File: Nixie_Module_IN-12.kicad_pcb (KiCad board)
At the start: 2 copper layers, 20 x 40 mm, 43 parts, among them J1 CONN_01X07, J3 CONN_01X02, J4 CONN_01X02, Q1 Q_NPN_BEC, Q10 Q_NPN_BEC, Q11 Q_NPN_BEC, Q2 Q_NPN_BEC, Q3 Q_NPN_BEC, Q4 Q_NPN_BEC, Q5 Q_NPN_BEC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

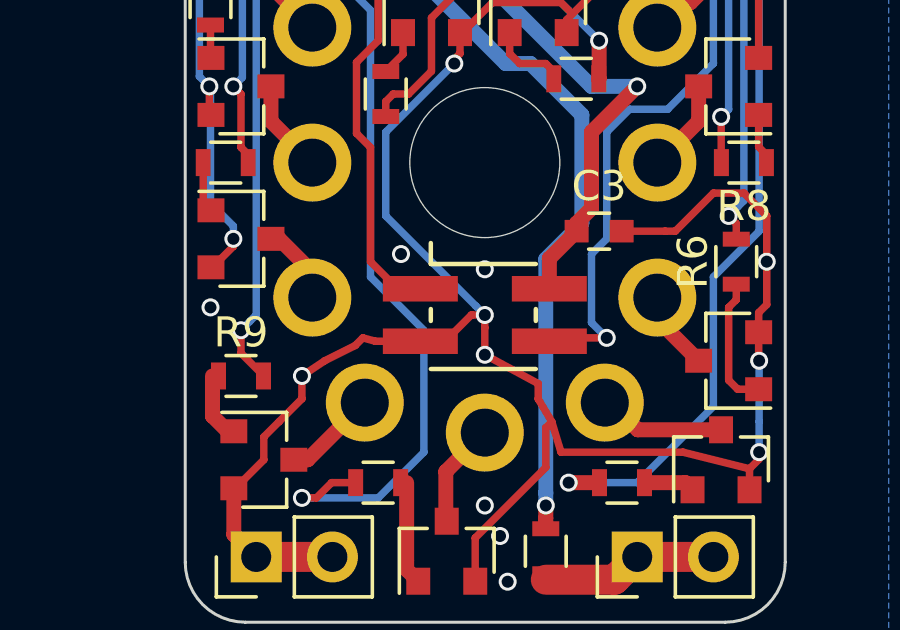
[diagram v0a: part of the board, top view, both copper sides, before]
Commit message: change to WS2812b
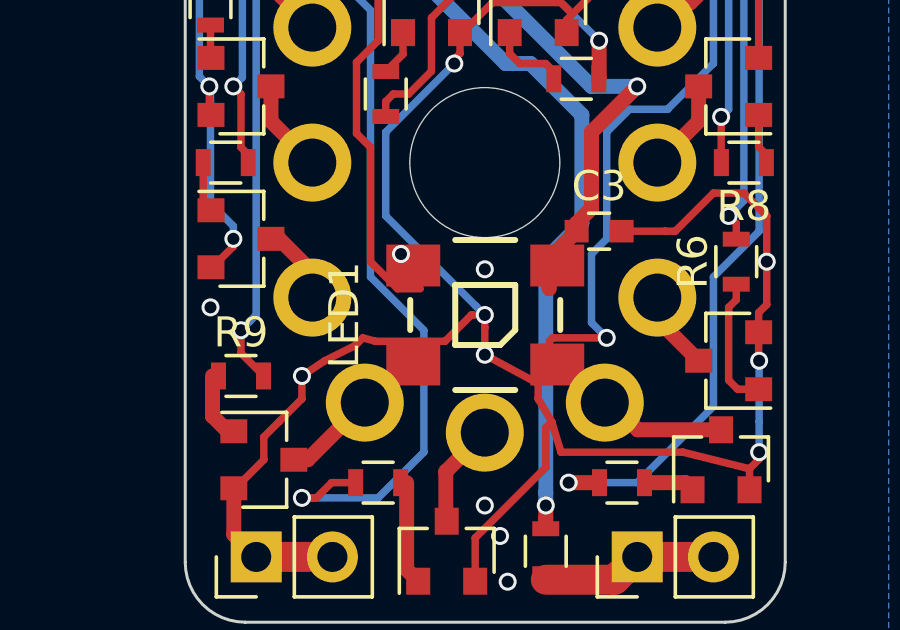
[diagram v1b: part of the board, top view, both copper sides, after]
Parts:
- removed U1: SK6812mini, FidgetSpinner:SK6812MINI
- added LED1: WS2812B, WS2812b:WS2812B, F.Cu at (79.3, 91.9)
- R1: value R -> 15k
- R14, R15, R16, R17, R18, R19, R2: value R -> 10k
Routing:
- net GND: vias 31 -> 30
- net +5V: vias 3 -> 4

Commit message: update footprint
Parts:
- LED1: value WS2812B -> VAL**
- moved LED1 0.25 mm to (79.3, 91.7), turned to 180 degrees
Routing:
- net +5V: track 51.3 -> 49.0 mm
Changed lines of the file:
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@@
     (thickness 1.6)
     (drawings 43)
-    (tracks 630)
+    (tracks 628)
     (zones 0)
     (modules 43)
@@
     (38 B.Mask user hide)
     (39 F.Mask user hide)
-    (40 Dwgs.User user hide)
+    (40 Dwgs.User user)
     (41 Cmts.User user hide)
     (42 Eco1.User user hide)
@@
     (add_net +HV)
   )
+  (module WS2812b:WS2812B (layer F.Cu)
+    (at 79.262 91.694 180)
+    (fp_text reference LED1 (at 0 -4.7 180) (layer F.SilkS)
+      (effects (font (size 1 1) (thickness 0.2)))
+    )
+    (fp_text value VAL** (at 0 4.8 180) (layer F.SilkS) hide
+      (effects (font (size 1 1) (thickness 0.2)))
+    )
+    (fp_line (start -2.49936 2.49936) (end -2.49936 -2.49936) (layer Dwgs.User) (width 0.2))
+    (fp_line (start 2.5 -2.5) (end 2.5 2.5) (layer Dwgs.User) (width 0.2))
+    (fp_line (start 2.1 2.7) (end 1.2 2.7) (layer Dwgs.User) (width 0.2))
+    (fp_line (start 2.1 1.8) (end 2.1 2.7) (layer Dwgs.User) (width 0.2))
+    (fp_line (start 1.2 1.8) (end 2.1 1.8) (layer Dwgs.User) (width 0.2))
+    (fp_line (start 1.2 2.7) (end 1.2 1.8) (layer Dwgs.User) (width 0.2))
+    (fp_line (start -1.2 2.7) (end -2.1 2.7) (layer Dwgs.User) (width 0.2))
+    (fp_line (start -1.2 1.8) (end -1.2 2.7) (layer Dwgs.User) (width 0.2))
+    (fp_line (start -2.1 1.8) (end -1.2 1.8) (layer Dwgs.User) (width 0.2))
+    (fp_line (start -2.1 2.7) (end -2.1 1.8) (layer Dwgs.User) (width 0.2))
+    (fp_line (start 2.1 -1.8) (end 2.1 -2.7) (layer Dwgs.User) (width 0.2))
+    (fp_line (start 1.2 -1.8) (end 2.1 -1.8) (layer Dwgs.User) (width 0.2))
+    (fp_line (start 1.2 -2.7) (end 1.2 -1.8) (layer Dwgs.User) (width 0.2))
+    (fp_line (start 2.1 -2.7) (end 1.2 -2.7) (layer Dwgs.User) (width 0.2))
+    (fp_line (start -2.1 -1.8) (end -2.1 -2.7) (layer Dwgs.User) (width 0.2))
+    (fp_line (start -1.2 -1.8) (end -2.1 -1.8) (layer Dwgs.User) (width 0.2))
+    (fp_line (start -1.2 -2.7) (end -1.2 -1.8) (layer Dwgs.User) (width 0.2))
+    (fp_line (start -2.1 -2.7) (end -1.2 -2.7) (layer Dwgs.User) (width 0.2))
+    (fp_line (start -2.5 -2.5) (end -2.1 -2.5) (layer Dwgs.User) (width 0.2))
+    (fp_line (start -1.2 -2.5) (end 1.2 -2.5) (layer Dwgs.User) (width 0.2))
+    (fp_line (start 2.1 -2.5) (end 2.5 -2.5) (layer Dwgs.User) (width 0.2))
+    (fp_line (start -2.5 2.5) (end -2.1 2.5) (layer Dwgs.User) (width 0.2))
+    (fp_line (start -1.2 2.5) (end 1.2 2.5) (layer Dwgs.User) (width 0.2))
+    (fp_line (start 2.1 2.5) (end 2.5 2.5) (layer Dwgs.User) (width 0.2))
+    (fp_line (start -0.5 -2.5) (end 0.5 -2.5) (layer F.SilkS) (width 0.2))
+    (fp_line (start 2.5 -1) (end 2.5 1) (layer F.SilkS) (width 0.2))
+    (fp_line (start -0.5 2.5) (end 0.5 2.5) (layer F.SilkS) (width 0.2))
+    (fp_line (start -2.5 -1) (end -2.5 1) (layer F.SilkS) (width 0.2))
+    (fp_line (start -1 0.5) (end -1 -1) (layer F.SilkS) (width 0.2))
+    (fp_line (start -0.5 1) (end -1 0.5) (layer F.SilkS) (width 0.2))
+    (fp_line (start 1 1) (end -0.5 1) (layer F.SilkS) (width 0.2))
+    (fp_line (start 1 -1) (end 1 1) (layer F.SilkS) (width 0.2))
+    (fp_line (start -1 -1) (end 1 -1) (layer F.SilkS) (width 0.2))
+    (pad 4 smd rect (at 1.65 2.4 180) (size 1 1.5) (layers F.Cu F.Paste F.Mask)
+      (net 42 /LED_DIN))
+    (pad 3 smd rect (at -1.65 2.4 180) (size 1 1.5) (layers F.Cu F.Paste F.Mask)
+      (net 2 GND))
+    (pad 2 smd rect (at -1.65 -2.4 180) (size 1 1.5) (layers F.Cu F.Paste F.Mask)
+      (net 43 /LED_DOUT))
+    (pad 1 smd rect (at 1.65 -2.4 180) (size 1 1.5) (layers F.Cu F.Paste F.Mask)
+      (net 1 +5V))
+  )
   (module R_SMD:R_0603 (layer F.Cu)
     (at 75.946 84.582 270)
@@
            (xy 0 0.75) (xy -0.5 0.75) (xy -0.5 -0.75) (xy 0 -0.75)) (width 0))
       ))
-  )
-  (module WS2812b:WS2812B (layer F.Cu)
-    (at 79.262 91.948 90)
-    (fp_text reference LED1 (at 0 -4.7 90) (layer F.SilkS)
-      (effects (font (size 1 1) (thickness 0.2)))
-    )
-    (fp_text value WS2812B (at 0 4.8 90) (layer F.SilkS) hide
-      (effects (font (size 1 1) (thickness 0.2)))
-    )
-    (fp_line (start -1 -1) (end 1 -1) (layer F.SilkS) (width 0.2))
-    (fp_line (start 1 -1) (end 1 1) (layer F.SilkS) (width 0.2))
-    (fp_line (start 1 1) (end -0.5 1) (layer F.SilkS) (width 0.2))
-    (fp_line (start -0.5 1) (end -1 0.5) (layer F.SilkS) (width 0.2))
-    (fp_line (start -1 0.5) (end -1 -1) (layer F.SilkS) (width 0.2))
-    (fp_line (start -2.5 -1) (end -2.5 1) (layer F.SilkS) (width 0.2))
-    (fp_line (start -0.5 2.5) (end 0.5 2.5) (layer F.SilkS) (width 0.2))
-    (fp_line (start 2.5 -1) (end 2.5 1) (layer F.SilkS) (width 0.2))
-    (fp_line (start -0.5 -2.5) (end 0.5 -2.5) (layer F.SilkS) (width 0.2))
-    (fp_line (start 2.1 2.5) (end 2.5 2.5) (layer Dwgs.User) (width 0.2))
-    (fp_line (start -1.2 2.5) (end 1.2 2.5) (layer Dwgs.User) (width 0.2))
-    (fp_line (start -2.5 2.5) (end -2.1 2.5) (layer Dwgs.User) (width 0.2))
-    (fp_line (start 2.1 -2.5) (end 2.5 -2.5) (layer Dwgs.User) (width 0.2))
-    (fp_line (start -1.2 -2.5) (end 1.2 -2.5) (layer Dwgs.User) (width 0.2))
-    (fp_line (start -2.5 -2.5) (end -2.1 -2.5) (layer Dwgs.User) (width 0.2))
-    (fp_line (start -2.1 -2.7) (end -1.2 -2.7) (layer Dwgs.User) (width 0.2))
-    (fp_line (start -1.2 -2.7) (end -1.2 -1.8) (layer Dwgs.User) (width 0.2))
-    (fp_line (start -1.2 -1.8) (end -2.1 -1.8) (layer Dwgs.User) (width 0.2))
-    (fp_line (start -2.1 -1.8) (end -2.1 -2.7) (layer Dwgs.User) (width 0.2))
-    (fp_line (start 2.1 -2.7) (end 1.2 -2.7) (layer Dwgs.User) (width 0.2))
-    (fp_line (start 1.2 -2.7) (end 1.2 -1.8) (layer Dwgs.User) (width 0.2))
-    (fp_line (start 1.2 -1.8) (end 2.1 -1.8) (layer Dwgs.User) (width 0.2))
-    (fp_line (start 2.1 -1.8) (end 2.1 -2.7) (layer Dwgs.User) (width 0.2))
-    (fp_line (start -2.1 2.7) (end -2.1 1.8) (layer Dwgs.User) (width 0.2))
-    (fp_line (start -2.1 1.8) (end -1.2 1.8) (layer Dwgs.User) (width 0.2))
-    (fp_line (start -1.2 1.8) (end -1.2 2.7) (layer Dwgs.User) (width 0.2))
-    (fp_line (start -1.2 2.7) (end -2.1 2.7) (layer Dwgs.User) (width 0.2))
-    (fp_line (start 1.2 2.7) (end 1.2 1.8) (layer Dwgs.User) (width 0.2))
-    (fp_line (start 1.2 1.8) (end 2.1 1.8) (layer Dwgs.User) (width 0.2))
-    (fp_line (start 2.1 1.8) (end 2.1 2.7) (layer Dwgs.User) (width 0.2))
-    (fp_line (start 2.1 2.7) (end 1.2 2.7) (layer Dwgs.User) (width 0.2))
-    (fp_line (start 2.5 -2.5) (end 2.5 2.5) (layer Dwgs.User) (width 0.2))
-    (fp_line (start -2.49936 2.49936) (end -2.49936 -2.49936) (layer Dwgs.User) (width 0.2))
-    (pad 1 smd rect (at 1.65 -2.4 90) (size 1.4 1.8) (layers F.Cu F.Paste F.Mask)
-      (net 1 +5V))
-    (pad 2 smd rect (at -1.65 -2.4 90) (size 1.4 1.8) (layers F.Cu F.Paste F.Mask)
-      (net 43 /LED_DOUT))
-    (pad 3 smd rect (at -1.65 2.4 90) (size 1.4 1.8) (layers F.Cu F.Paste F.Mask)
-      (net 2 GND))
-    (pad 4 smd rect (at 1.65 2.4 90) (size 1.4 1.8) (layers F.Cu F.Paste F.Mask)
-      (net 42 /LED_DIN))
   )
   (gr_text ADDR3 (at 75.184 75.438) (layer B.SilkS)
@@
   (segment (start 74.168 72.644) (end 74.676 72.644) (width 0.25) (layer F.Cu) (net 1))
   (segment (start 73.356 72.644) (end 74.168 72.644) (width 0.25) (layer F.Cu) (net 1))
-  (segment (start 81.398 90.064) (end 82.308 89.154) (width 0.5) (layer F.Cu) (net 1) (status 20))
-  (segment (start 81.398 91.073) (end 81.398 90.064) (width 0.5) (layer F.Cu) (net 1))
   (segment (start 82.308 88.912) (end 82.308 89.154) (width 0.5) (layer F.Cu) (net 1) (status 30))
   (segment (start 82.296 88.9) (end 82.308 88.912) (width 0.5) (layer F.Cu) (net 1) (status 30))
@@
   (segment (start 76.454 76.624264) (end 76.454 76.2) (width 0.5) (layer B.Cu) (net 1))
   (via (at 76.454 76.2) (size 0.6) (drill 0.4) (layers F.Cu B.Cu) (net 1))
+  (via (at 76.454 89.916) (size 0.6) (drill 0.4) (layers F.Cu B.Cu) (net 1) (status 30))
   (segment (start 70.47 76.312) (end 70.47 75.692) (width 0.25) (layer B.Cu) (net 2) (status 20))
   (segment (start 77.877 68.27) (end 77.227 68.27) (width 0.25) (layer F.Cu) (net 2) (status 30))
@@
   (via (at 79.248 90.424) (size 0.6) (drill 0.4) (layers F.Cu B.Cu) (net 2))
   (via (at 79.248 93.273002) (size 0.6) (drill 0.4) (layers F.Cu B.Cu) (net 2))
-  (via (at 76.454 89.916) (size 0.6) (drill 0.4) (layers F.Cu B.Cu) (net 1))
   (via (at 87.884 72.644) (size 0.6) (drill 0.4) (layers F.Cu B.Cu) (net 2))
   (segment (start 88.646 90.17) (end 88.646 88.646) (width 0.25) (layer F.Cu) (net 2))
@@
   (segment (start 81.28 97.028) (end 78.928 99.38) (width 0.25) (layer F.Cu) (net 2))
   (segment (start 81.026 94.742) (end 81.478998 95.504) (width 0.25) (layer F.Cu) (net 2))
-  (segment (start 79.248 93.273002) (end 81.026 94.234) (width 0.25) (layer F.Cu) (net 2))
-  (segment (start 81.026 94.234) (end 81.026 94.742) (width 0.25) (layer F.Cu) (net 2))
+  (segment (start 79.248 93.273002) (end 81.026 94.234) (width 0.25) (layer F.Cu) (net 2) (status 20))
+  (segment (start 81.026 94.234) (end 81.026 94.742) (width 0.25) (layer F.Cu) (net 2) (status 10))
   (segment (start 81.788 96.52) (end 81.478998 95.504) (width 0.25) (layer F.Cu) (net 2))
   (segment (start 88.072 97.074) (end 85.852 96.52) (width 0.25) (layer F.Cu) (net 2))
